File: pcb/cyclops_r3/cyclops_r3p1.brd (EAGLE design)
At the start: 69.8 x 53.3 mm, 59 parts, among them Q1 SUM11006, Q2 IRF510, U1 MCP4921, U2 317-N, U3 ADR03, U4 OP1177, U5 LM324N, U6 ZXTD45

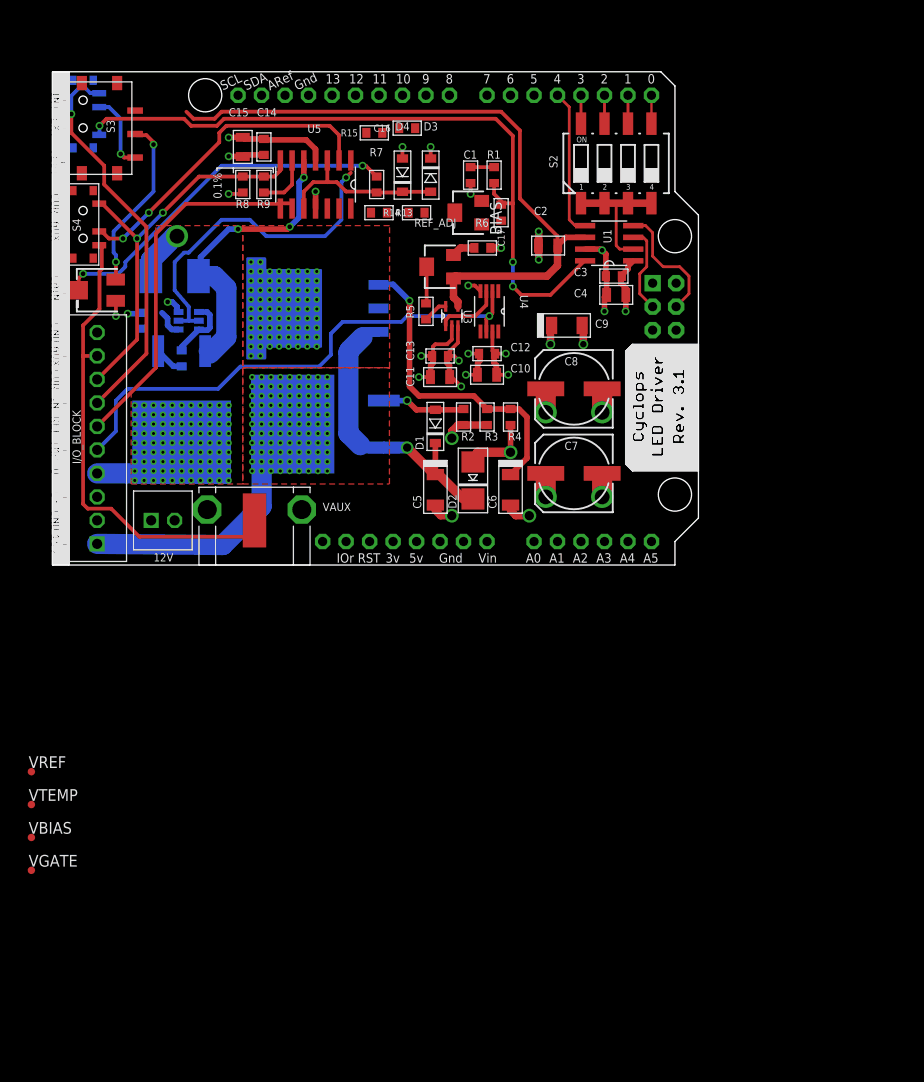
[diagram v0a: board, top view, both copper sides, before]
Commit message: Substantial changes to the layout of the analog frontend of the circuit.
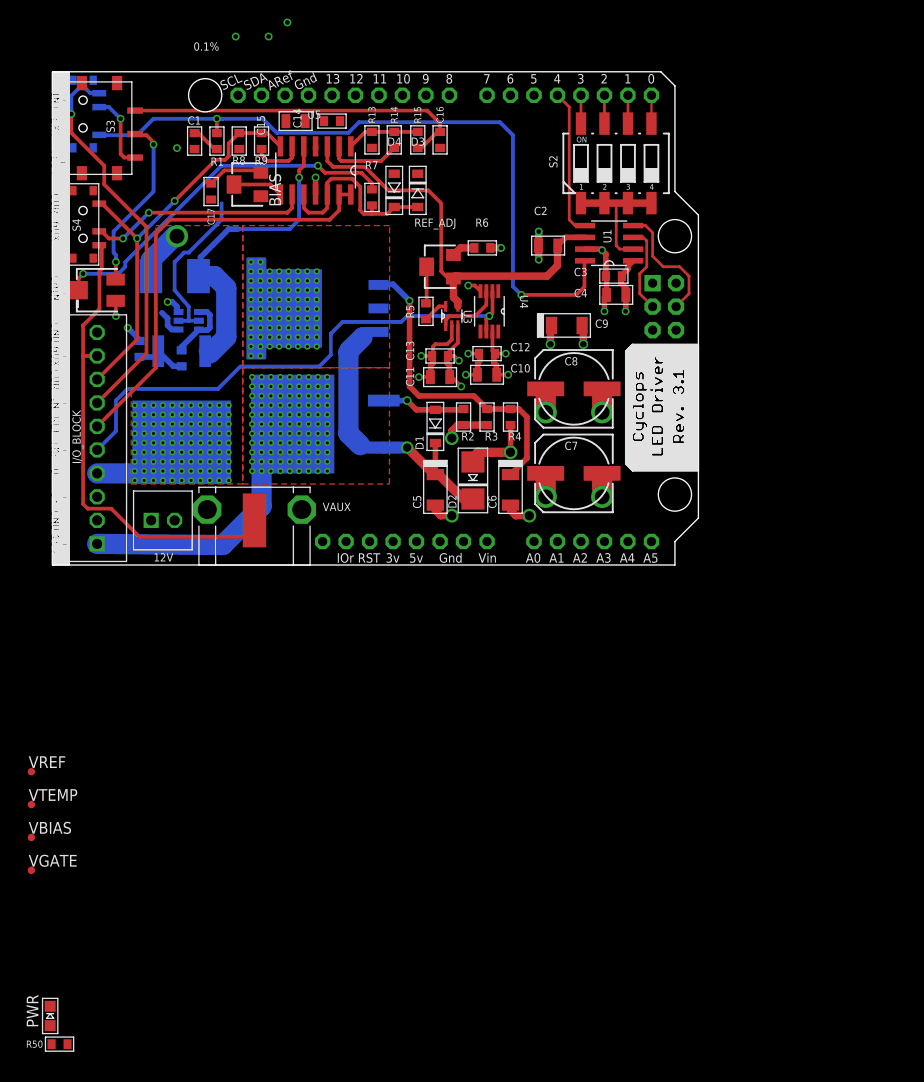
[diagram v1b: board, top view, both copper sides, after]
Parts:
- added PWR: (no value), cyclops:CHIP-LED0805
- added R50: 2.4k, cyclops:0603
- moved C17 31.5 mm to (15.9, 40.4)
- moved R1 30.2 mm to (16.5, 45.8), turned to 90 degrees
- moved C1 30.1 mm to (14.1, 45.8)
- moved BIAS 24.1 mm to (19.8, 41.1)
- moved R14 8.24 mm to (35.7, 46.0), turned to 270 degrees
- moved R13 7.91 mm to (33.3, 46.0), turned to 270 degrees
- moved C14 7.88 mm to (29.0, 48.0), turned to 0 degrees
- moved C15 6.36 mm to (25.0, 48.0), turned to 0 degrees
- moved R15 4.76 mm to (38.2, 46.0), turned to 270 degrees
- moved R8 4.71 mm to (18.9, 45.8)
- moved R9 4.71 mm to (21.3, 45.8)
- moved C16 3.78 mm to (40.6, 46.0), turned to 270 degrees
- moved R12 3.06 mm to (8.13, 23.4)
- moved D3 2.16 mm to (38.2, 40.5)
- moved D4 1.88 mm to (35.7, 40.5)
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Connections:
- net VREF2X renamed REFA2X
- new net N$3: PWR.A, R50.1
- new net REFA: C2.1, REF_ADJ.1, U1.6, U3.4, U5.3, VREF.TP
- net +12V: now also R50.2
- net GND: now also PWR.C
- net N$4: now also U5.8; no longer U5.1
- net N$8: now also U5.2; no longer U5.13
- net VFB: now also U5.9; no longer U5.2
- net VREF: now also U5.13, U5.14; no longer C2.1, REF_ADJ.1, U1.6, U3.4, U5.12, U5.8, U5.9, VREF.TP
- net VREFA2X: now also U5.1; no longer U5.14
- net _VREF: now also U5.12; no longer U5.3
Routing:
- net VREF: track 113.5 -> 47.3 mm
- net REFA: track 0.00 -> 45.9 mm
- net REFA2X: track 0.00 -> 37.6 mm
- net N$4: track 36.2 -> 23.5 mm, vias 1 -> 0
- net +12V: track 47.7 -> 35.6 mm, vias 86 -> 85
- net VFB: track 35.1 -> 24.0 mm
- net N$8: track 0.00 -> 7.99 mm
- net VREFA2X: track 0.00 -> 7.89 mm
- net GND: track 67.9 -> 60.1 mm, vias 25 -> 24
- net AGND: track 0.00 -> 6.08 mm
- net N$13: track 3.22 -> 5.81 mm
- net _VREF: track 18.8 -> 21.4 mm
- net VI: track 42.3 -> 44.3 mm
- net N$2: track 33.1 -> 34.8 mm, vias 3 -> 1
- net N$1: track 2.54 -> 3.13 mm
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
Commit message: Almost finished with layout changes. Added not concerning over current protection.
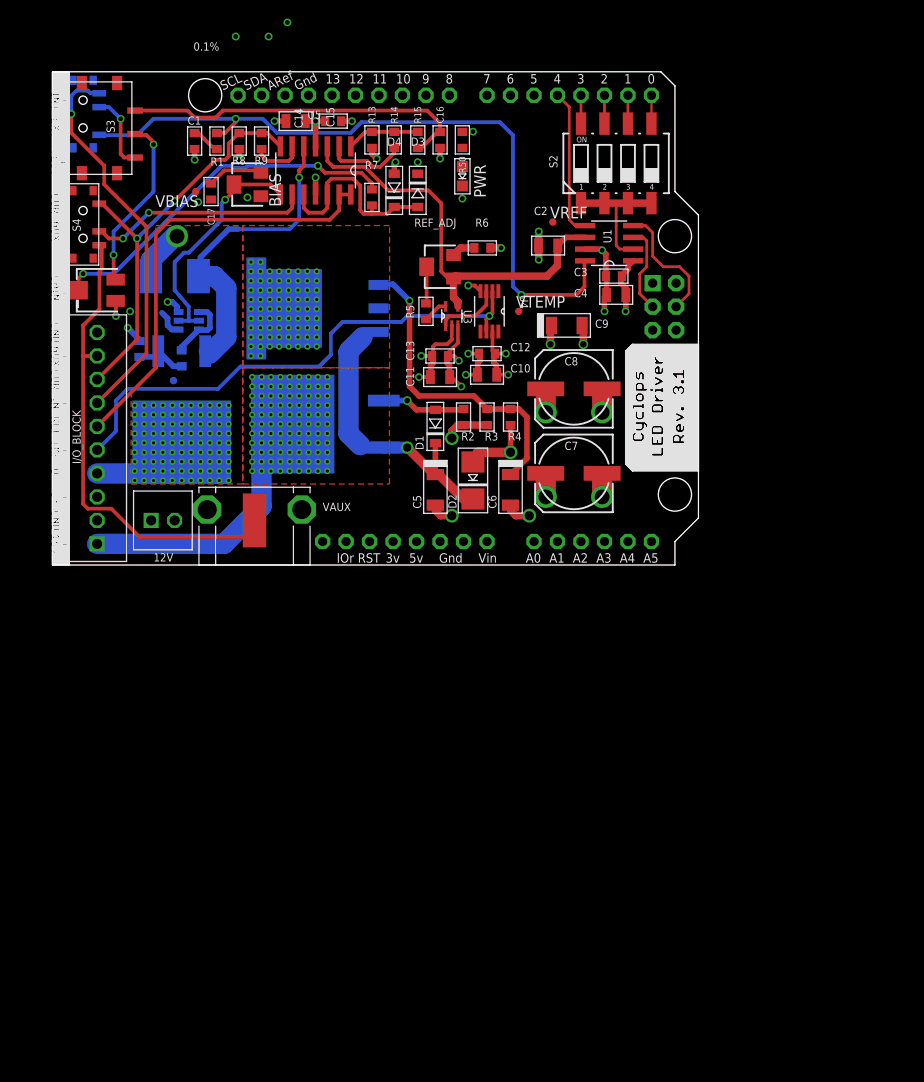
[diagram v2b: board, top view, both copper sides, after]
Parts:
- moved R50 107.1 mm to (43.1, 46.0), turned to 90 degrees
- moved PWR 101.2 mm to (43.1, 42.0), turned to 180 degrees
- moved VREF 81.9 mm to (52.8, 37.1)
- moved VTEMP 75.0 mm to (49.1, 27.4)
- moved VBIAS 72.1 mm to (14.2, 40.4), turned to 180 degrees
- moved VGATE 55.1 mm to (11.8, 19.9), flipped to the bottom
- moved C14 0.13 mm to (29.1, 48.0)
- turned C15 to 180 degrees
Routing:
- net GND: track 60.1 -> 68.7 mm, vias 24 -> 31
- net +12V: track 35.6 -> 40.5 mm, vias 85 -> 91
- net N$4: track 23.5 -> 26.0 mm, vias 0 -> 1
- net DACA: track 76.5 -> 77.8 mm
- net N$8: track 7.99 -> 8.83 mm
- net REFA2X: track 37.6 -> 38.2 mm

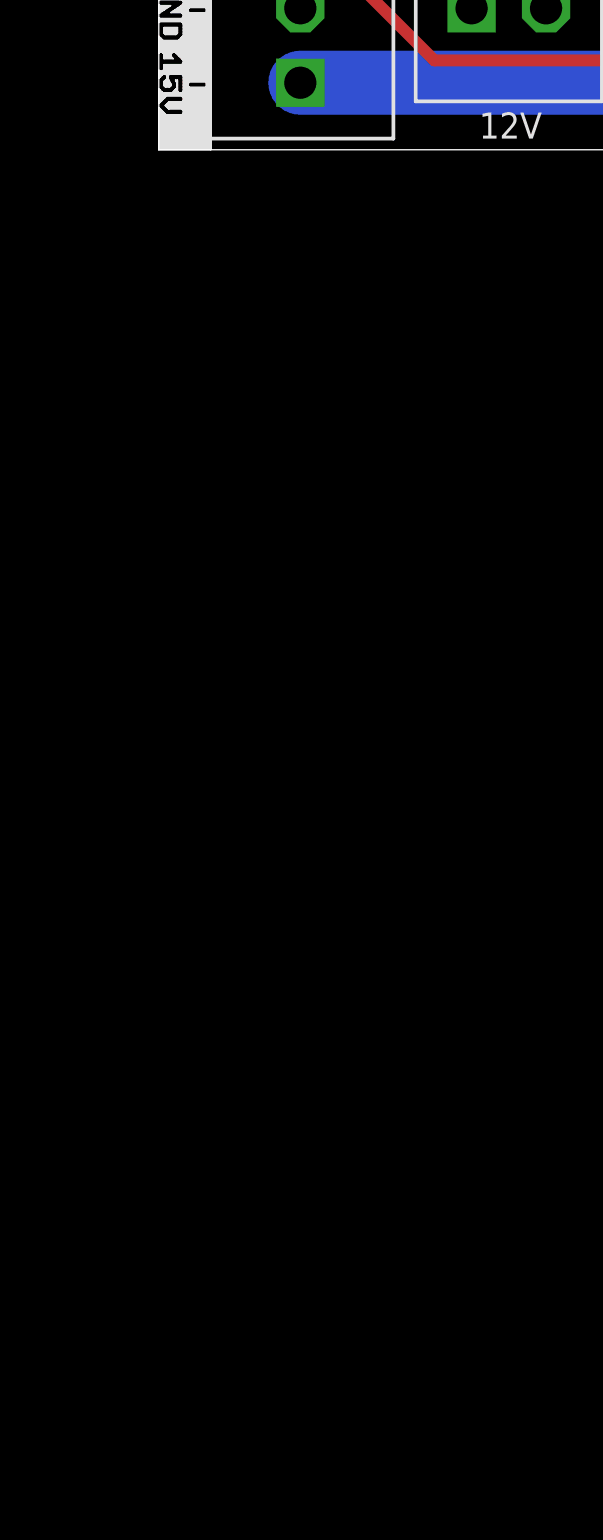
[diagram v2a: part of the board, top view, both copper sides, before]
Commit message: Added an overcurrent kill circuit. This needs to be tested. Also, a reset switch needs to be added.
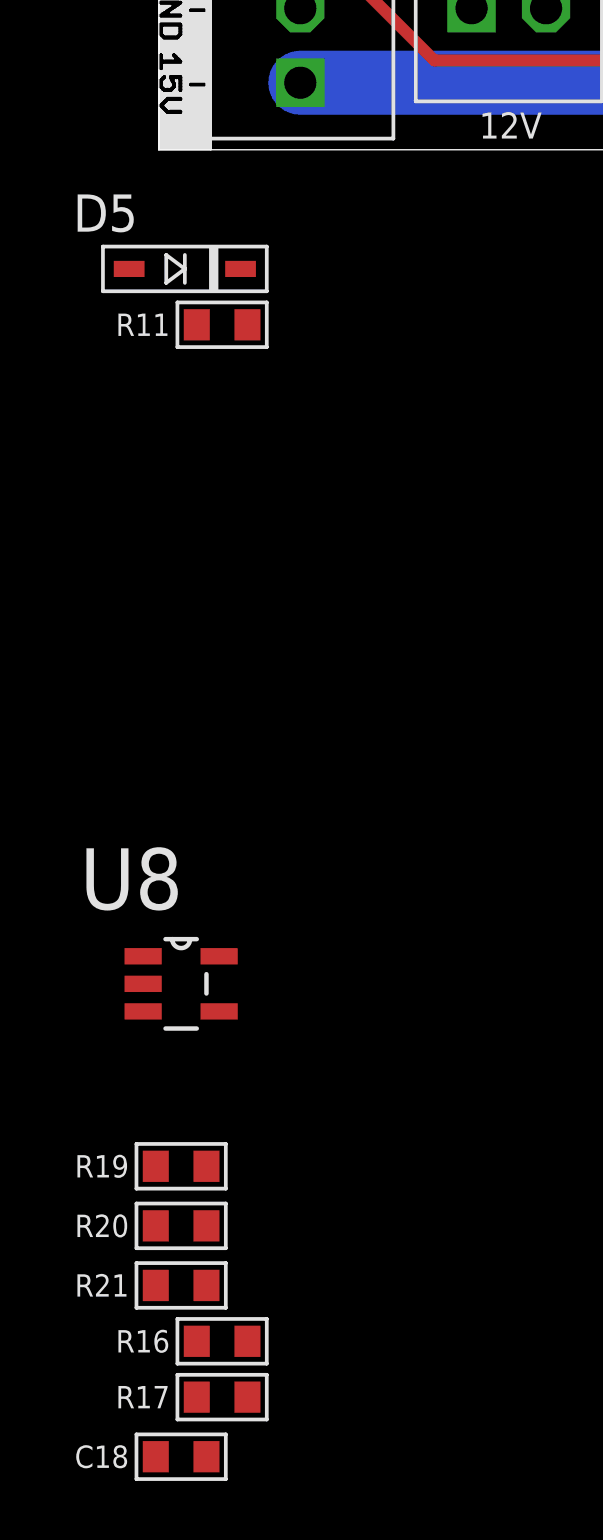
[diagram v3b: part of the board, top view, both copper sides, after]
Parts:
- added C18: .1uF, cyclops:0603
- added D5: (no value), cyclops:SOD-323F
- added R11, R21: 220k, cyclops:0603
- added R16: 120k, cyclops:0603
- added R17: 1k, cyclops:0603
- added R19: 4k, cyclops:0603
- added R20: 56k, cyclops:0603
- added U8: TLV3701CDBVT, ti-extended:SOT95P280X145-5N
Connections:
- new net KILL: D5.A, R11.2, R17.1, U8.1
- new net N$14: R16.1, R21.2, U8.3
- new net N$5: R19.1, R20.2, U8.4
- new net N$9: R17.2, R21.1
- net +15V: now also C18.1, R20.1, U8.5
- net GND: now also C18.2, R11.1, R19.2, U8.2
- net N$18: now also D5.C
- net VI: now also R16.2

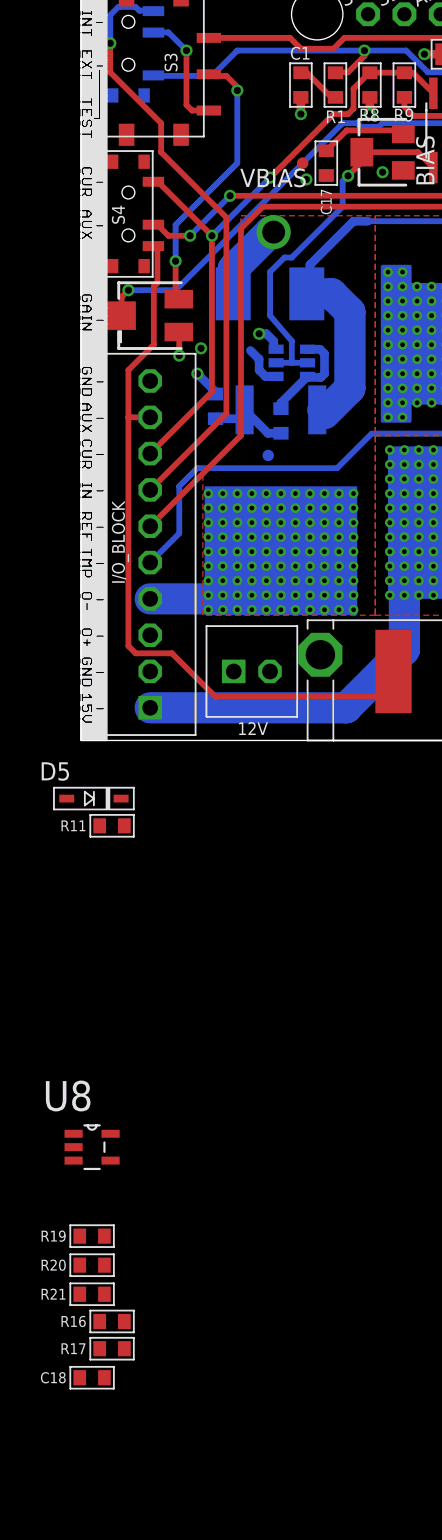
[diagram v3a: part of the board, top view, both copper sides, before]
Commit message: Modifications to overcurrent protection allow 2A max, and lights alarm LED.
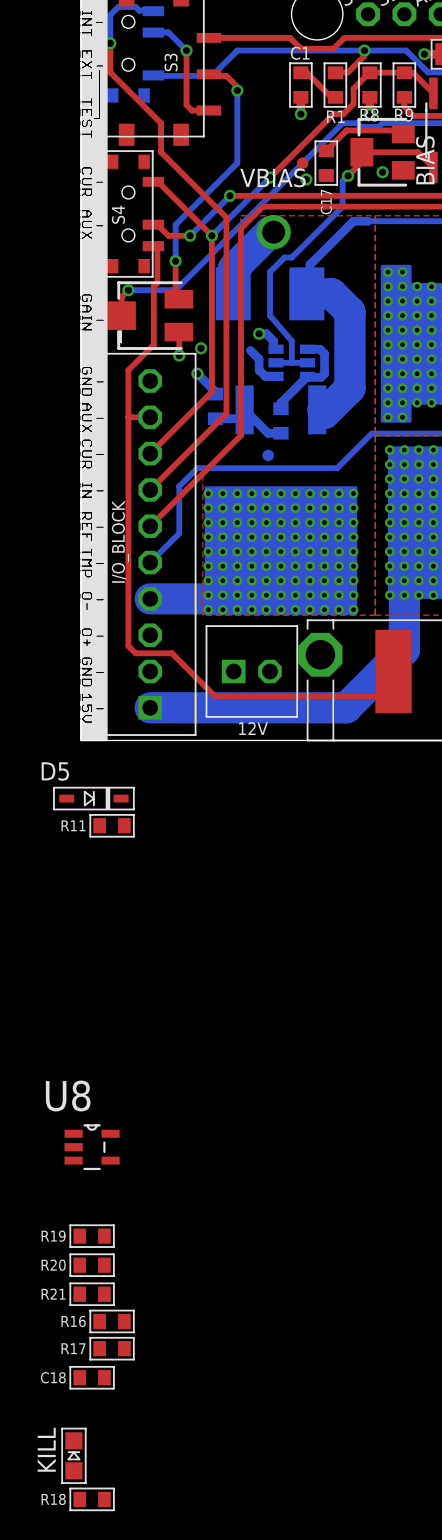
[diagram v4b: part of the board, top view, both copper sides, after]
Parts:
- added KILL: (no value), cyclops:CHIP-LED0805
- added R18: 3.0k, cyclops:0603
- R16: value 120k -> 100k
- R21: value 220k -> 91k
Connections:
- new net N$11: KILL.A, R18.1
- net GND: now also KILL.C
- net KILL: now also R18.2

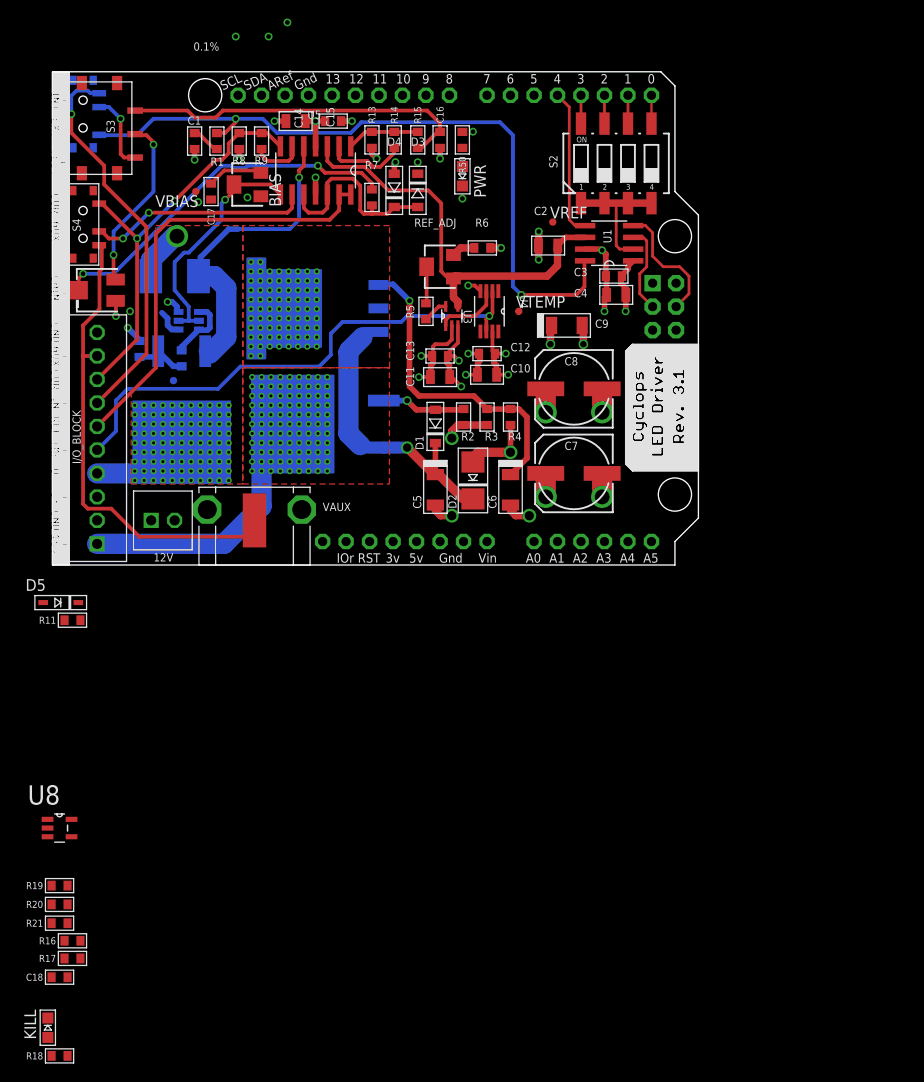
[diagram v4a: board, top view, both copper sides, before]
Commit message: Started implementing the over curren protection circuit on the board.
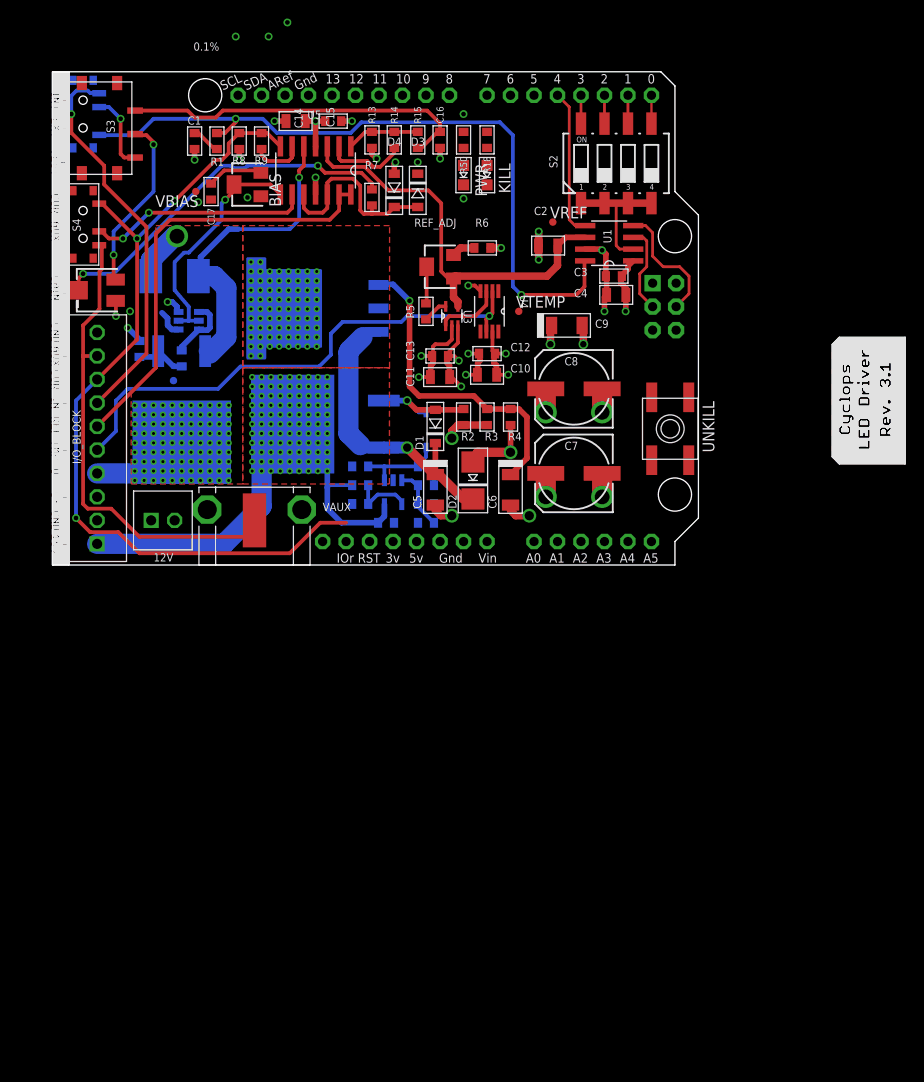
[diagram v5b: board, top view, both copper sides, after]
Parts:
- added C19: 10pF, cyclops:0603
- added UNKILL: SPST_TACT-EVQQ2, cyclops:EVQ-Q2
- moved R18 109.3 mm to (45.7, 46.0), turned to 90 degrees
- moved KILL 103.7 mm to (45.7, 42.2), turned to 180 degrees
- moved R17 65.5 mm to (39.1, 10.7), flipped to the bottom, turned to 180 degrees
- moved R21 61.8 mm to (39.1, 8.64), flipped to the bottom
- moved C18 60.5 mm to (34.8, 4.57), flipped to the bottom, turned to 180 degrees
- moved R16 59.2 mm to (39.1, 4.57), flipped to the bottom
- moved R20 55.8 mm to (32.0, 8.64), flipped to the bottom, turned to 180 degrees
- moved R19 52.5 mm to (32.0, 6.60), flipped to the bottom
- moved U8 51.2 mm to (35.6, 7.87), flipped to the bottom, turned to 270 degrees
- moved D5 43.7 mm to (39.1, 14.6), flipped to the bottom, turned to 90 degrees
- moved R11 35.3 mm to (32.0, 10.7), flipped to the bottom, turned to 180 degrees
- moved PWR 0.18 mm to (43.2, 42.2)
- moved R50 0.13 mm to (43.2, 46.0)
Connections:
- removed net N$14: R16.1, R21.2, U8.3
- new net COMP+: C19.1, R16.1, R21.2, U8.3, UNKILL.A, UNKILL.A'
- net AGND: now also UNKILL.B, UNKILL.B'
- net GND: now also C19.2
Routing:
- net VI: track 44.1 -> 92.2 mm, vias 2 -> 3
- net +15V: track 31.9 -> 47.2 mm
- net KILL: track 0.00 -> 9.28 mm
- net COMP+: track 0.00 -> 6.77 mm
- net N$5: track 0.00 -> 6.72 mm
- net N$18: track 9.07 -> 11.6 mm
- net N$9: track 0.00 -> 2.03 mm
